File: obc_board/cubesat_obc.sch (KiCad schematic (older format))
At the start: 10 parts, among them J1 Conn_01x08_Female, J2 Conn_01x05_Female, J3 Conn_01x04_Female, J4 Conn_01x04_Female

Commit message: modify planes
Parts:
- renumbered J3 to ADC0, J4 to ADC1, J2 to SPI0, J1 to UART_FTDI0
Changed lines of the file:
@@
 $Descr A4 11693 8268
 encoding utf-8
-Sheet 1 8
+Sheet 1 9
 Title ""
 Date ""
@@
 S 1400 2300 1350 1100
 U 5F315FB6
-F0 "sensors" 50
-F1 "sensors.sch" 50
+F0 "temp_sensors" 50
+F1 "temp_sensors.sch" 50
 F2 "3V3" I L 1400 2500 50
 F3 "GND" I L 1400 2600 50
@@
 	7700 1150 8300 1150
 $Comp
-L Connector:Conn_01x04_Female J3
+L Connector:Conn_01x04_Female ADC0
 U 1 1 5F6F0159
 P 4400 7100
-F 0 "J3" H 4428 7076 50  0000 L CNN
+F 0 "ADC0" H 4428 7076 50  0000 L CNN
 F 1 "Conn_01x04_Female" H 4428 6985 50  0000 L CNN
 F 2 "Connector_Molex:Molex_PicoBlade_53261-0471_1x04-1MP_P1.25mm_Horizontal" H 4400 7100 50  0001 C CNN
@@
 	3700 7150 3700 7000
 $Comp
-L Connector:Conn_01x04_Female J4
+L Connector:Conn_01x04_Female ADC1
 U 1 1 5F6F5054
 P 6100 7100
-F 0 "J4" H 6128 7076 50  0000 L CNN
+F 0 "ADC1" H 6128 7076 50  0000 L CNN
 F 1 "Conn_01x04_Female" H 6128 6985 50  0000 L CNN
 F 2 "Connector_Molex:Molex_PicoBlade_53261-0471_1x04-1MP_P1.25mm_Horizontal" H 6100 7100 50  0001 C CNN
@@
 3V3_P
 $Comp
-L Connector:Conn_01x05_Female J2
+L Connector:Conn_01x05_Female SPI0
 U 1 1 5F3493AD
 P 7250 3050
-F 0 "J2" H 7278 3076 50  0000 L CNN
+F 0 "SPI0" H 7278 3076 50  0000 L CNN
 F 1 "Conn_01x05_Female" H 7278 2985 50  0000 L CNN
 F 2 "Connector_Molex:Molex_PicoBlade_53261-0571_1x05-1MP_P1.25mm_Horizontal" H 7250 3050 50  0001 C CNN
@@
 P 3200 6900
 AR Path="/5E7EC636/5F5D669F" Ref="J?"  Part="1"
-AR Path="/5F5D669F" Ref="J1"  Part="1"
-F 0 "J1" H 3092 6275 50  0000 C CNN
+AR Path="/5F5D669F" Ref="UART_FTDI0"  Part="1"
+F 0 "UART_FTDI0" H 3092 6275 50  0000 C CNN
 F 1 "Conn_01x08_Female" H 3092 6366 50  0000 C CNN
 F 2 "Connector_Molex:Molex_PicoBlade_53261-0871_1x08-1MP_P1.25mm_Horizontal" H 3200 6900 50  0001 C CNN
@@
 Text Label 3050 5600 0    50   ~ 0
 FAULT4
+$Sheet
+S 6750 5400 850  800
+U 5F9EB759
+F0 "imu" 50
+F1 "imu.sch" 50
+$EndSheet
 $EndSCHEMATC

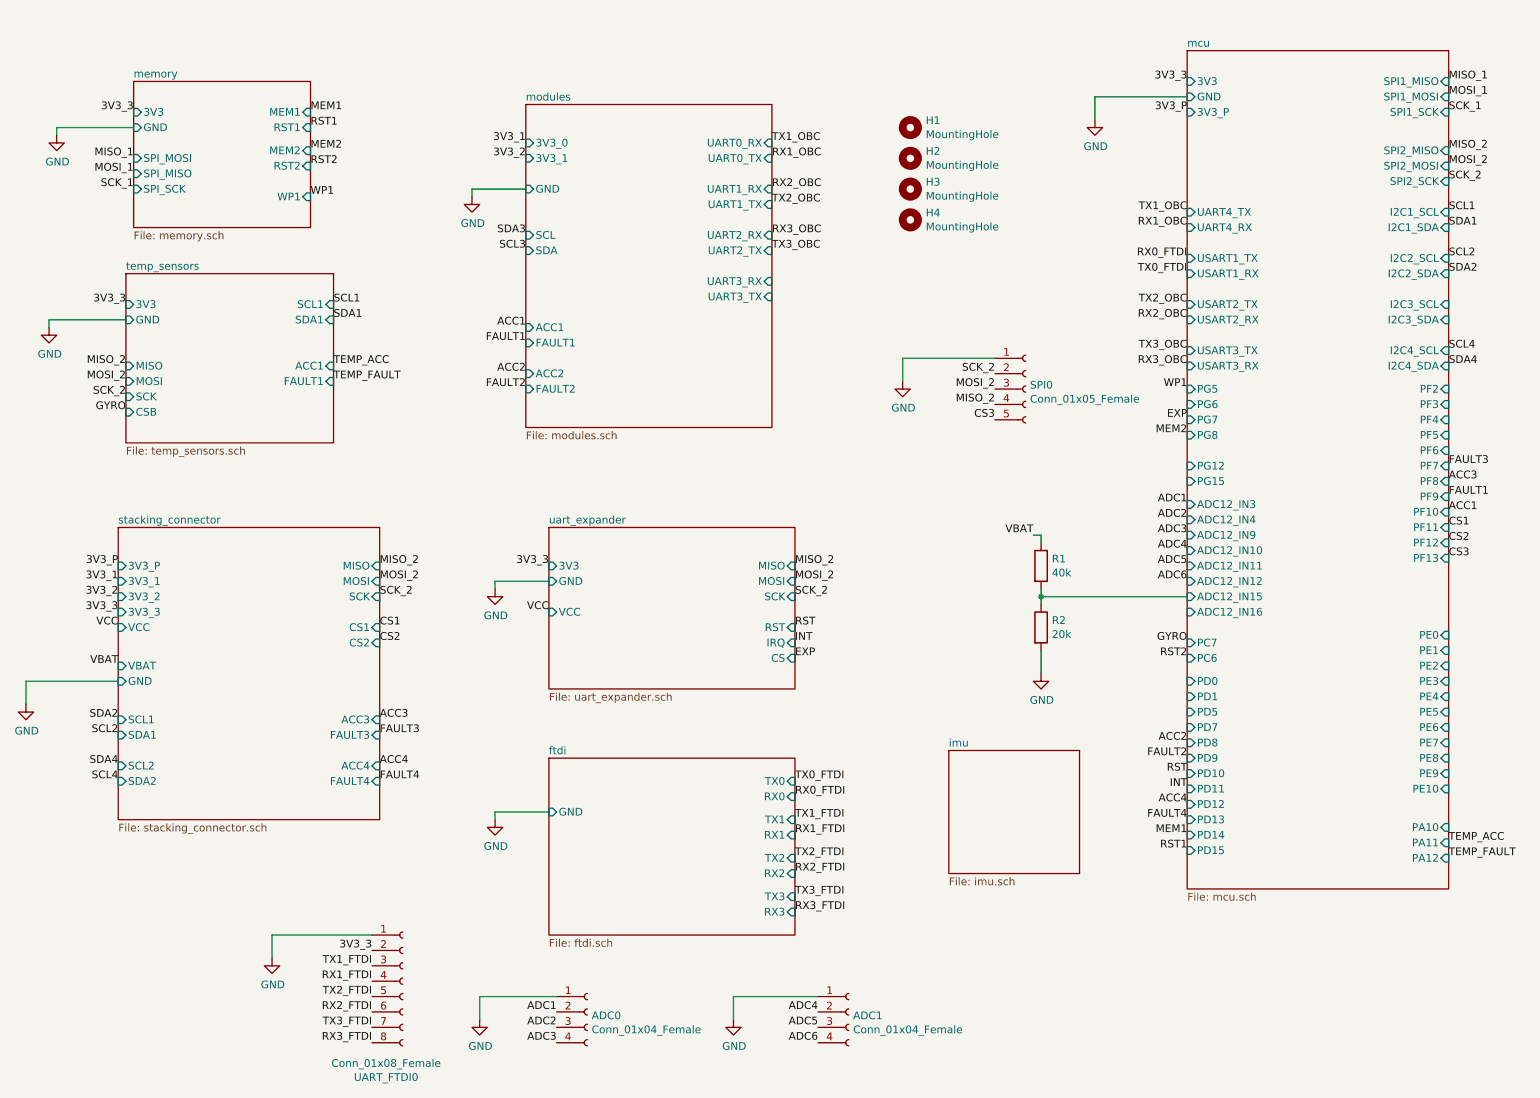
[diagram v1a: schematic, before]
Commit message: add imu and mux
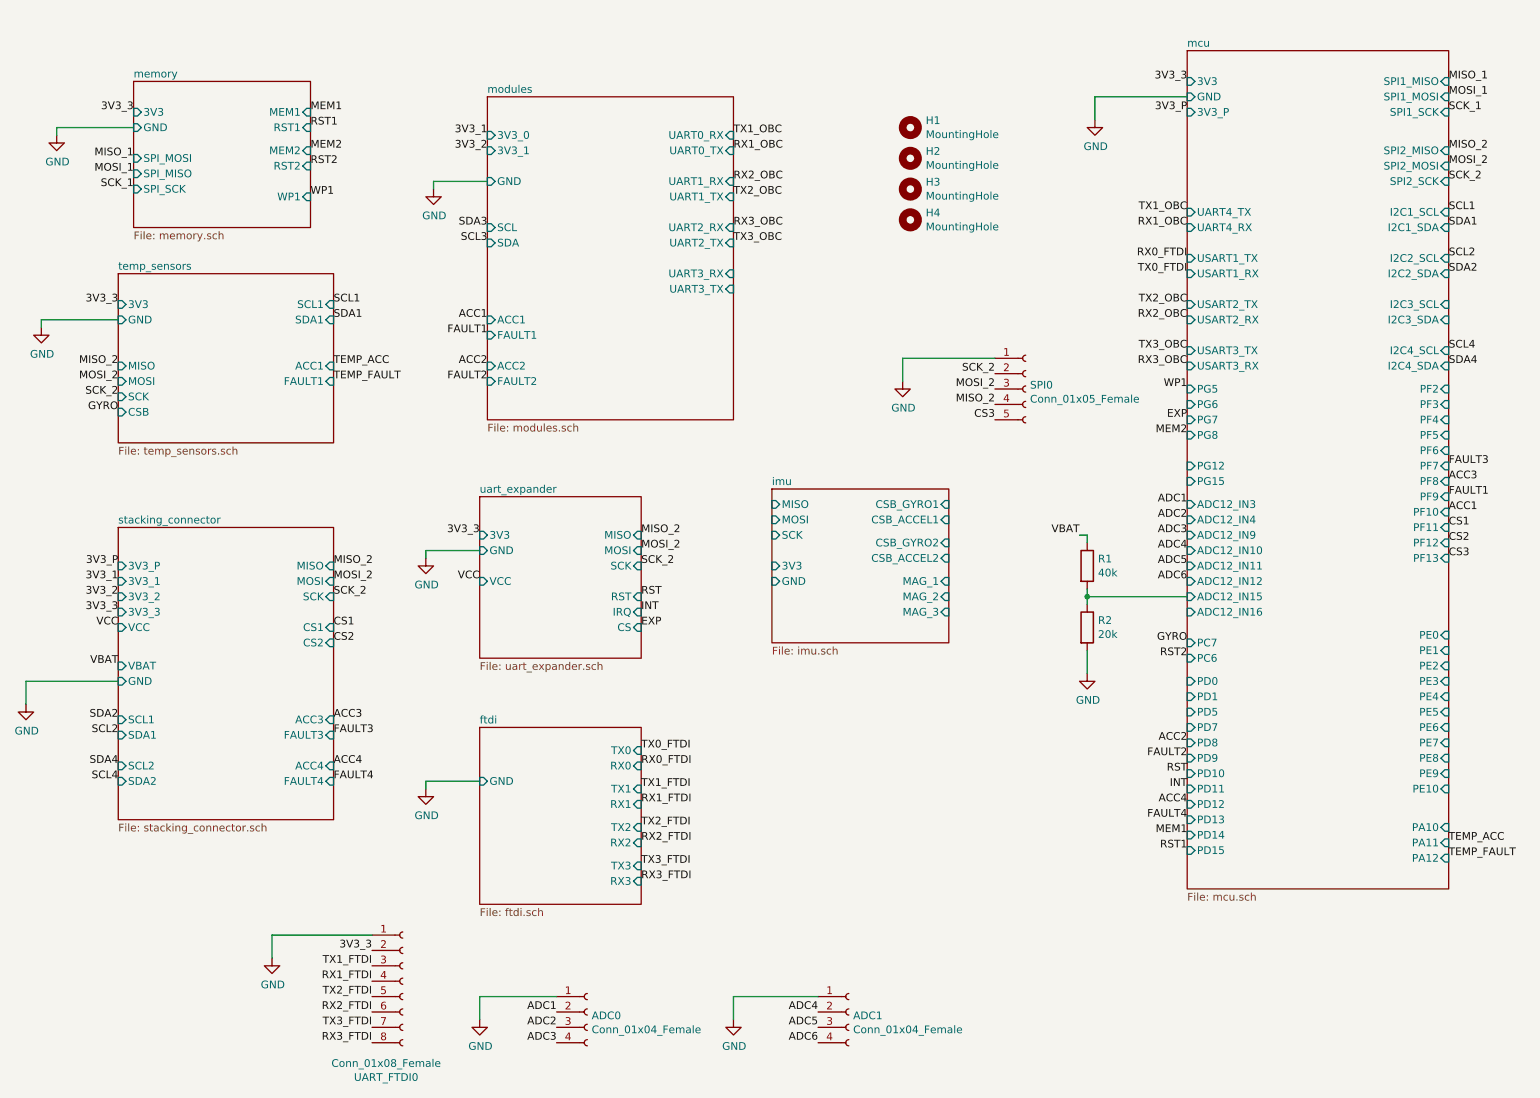
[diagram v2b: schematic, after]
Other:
- moved on the sheet: R1, R2

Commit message: added h bridge and magnetometers
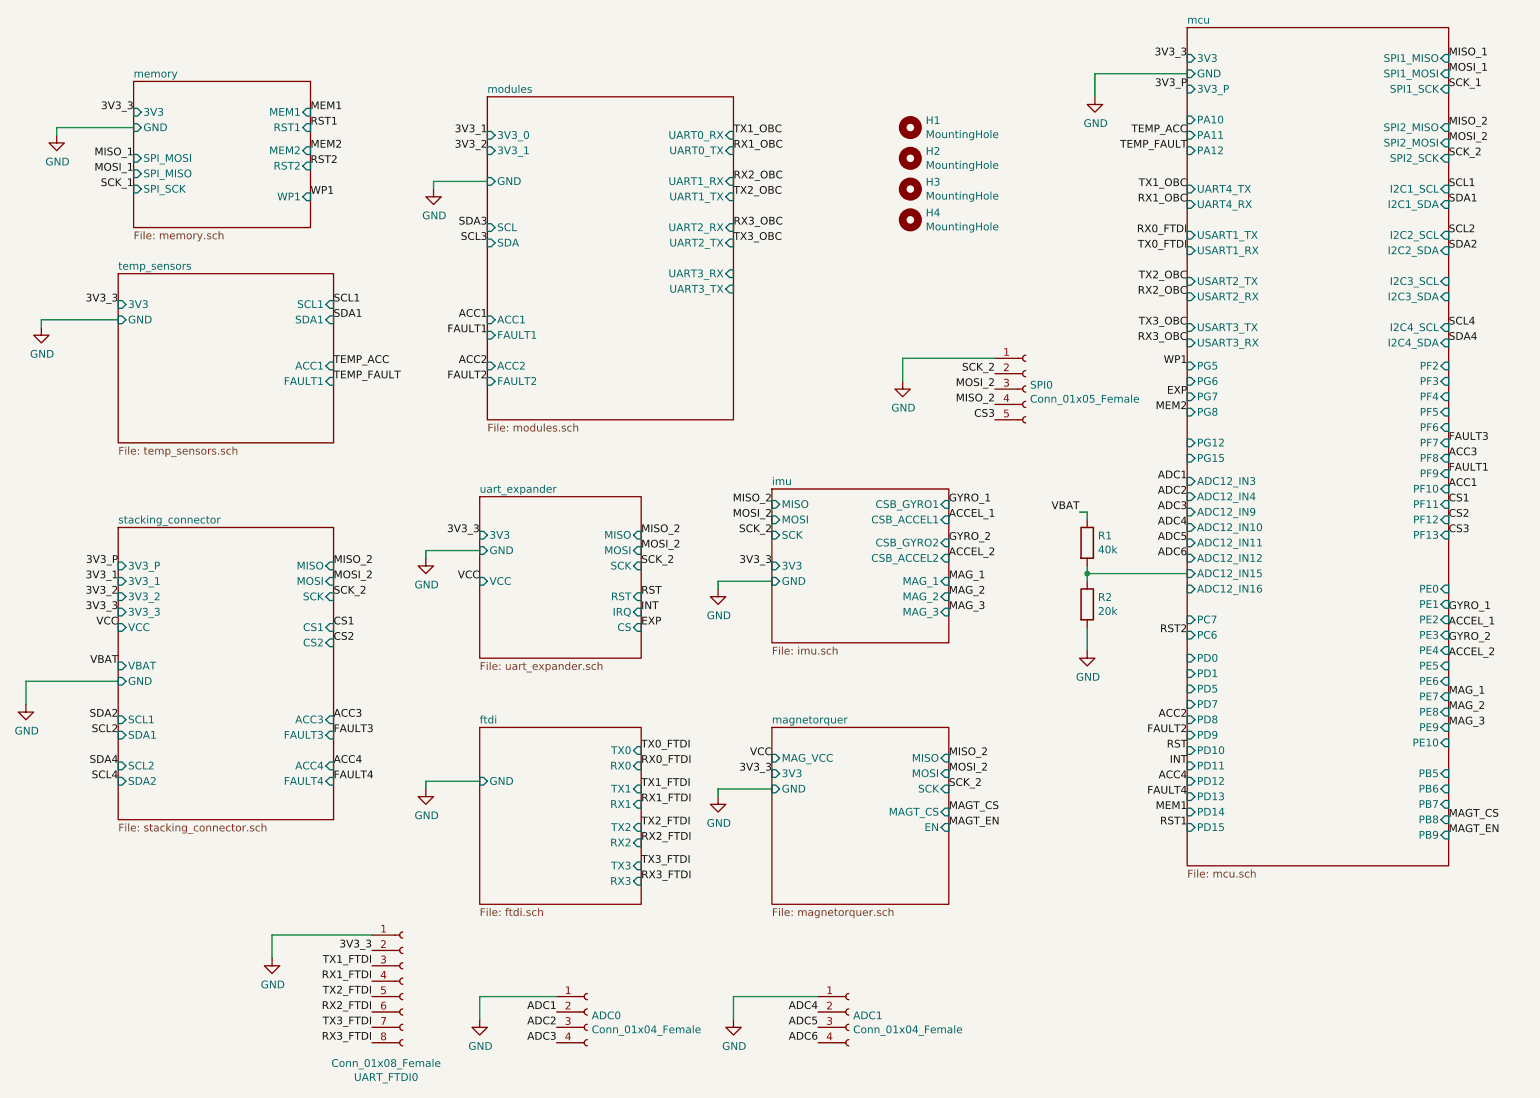
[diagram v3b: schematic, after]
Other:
- moved on the sheet: R1, R2

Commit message: reroute
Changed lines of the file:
@@
 F2 "3V3" I L 1350 2500 50
 F3 "GND" I L 1350 2600 50
-F8 "SCL1" I R 2750 2500 50
-F9 "SDA1" I R 2750 2600 50
-F10 "ACC1" I R 2750 2900 50
-F11 "FAULT1" I R 2750 3000 50
+F4 "SCL1" I R 2750 2500 50
+F5 "SDA1" I R 2750 2600 50
+F6 "ACC1" I R 2750 2900 50
+F7 "FAULT1" I R 2750 3000 50
 $EndSheet
 $Sheet
@@
 Text Label 2750 2900 0    50   ~ 0
 TEMP_ACC
-Text Label 8300 1400 2    50   ~ 0
+Text Label 8300 4800 2    50   ~ 0
 TEMP_ACC
 Text Label 2750 3000 0    50   ~ 0
 TEMP_FAULT
-Text Label 8300 1500 2    50   ~ 0
+Text Label 8300 4900 2    50   ~ 0
 TEMP_FAULT
 Text Label 3750 2600 2    50   ~ 0

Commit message: rerouted
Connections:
- net MISO_2: now also SPI0.2 (Pin_2); no longer SPI0.4 (Pin_4)
- net SCK_2: now also SPI0.4 (Pin_4); no longer SPI0.2 (Pin_2)
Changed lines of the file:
@@
 F18 "UART3_TX" I R 5350 2400 50
 $EndSheet
-Text Label 8300 5800 2    50   ~ 0
+Text Label 8300 2900 2    50   ~ 0
 MEM1
-Text Label 8300 3200 2    50   ~ 0
+Text Label 8300 3100 2    50   ~ 0
 MEM2
 Text Label 2600 1250 0    50   ~ 0
@@
 Text Label 8300 4650 2    50   ~ 0
 RST2
-Text Label 8300 2900 2    50   ~ 0
+Text Label 8300 5900 2    50   ~ 0
 WP1
-Text Label 8300 5900 2    50   ~ 0
+Text Label 8300 3000 2    50   ~ 0
 RST1
 Text Label 2600 1350 0    50   ~ 0
@@
 F 1 "Conn_01x04_Female" H 4428 6985 50  0000 L CNN
 F 2 "Connector_Molex:Molex_PicoBlade_53261-0471_1x04-1MP_P1.25mm_Horizontal" H 4400 7100 50  0001 C CNN
-F 3 "https://www.molex.com/pdm_docs/sd/532610471_sd.pdf" H 4400 7100 50  0001 C CNN
+F 3 "~" H 4400 7100 50  0001 C CNN
 F 4 "WM7622CT-ND" H 4400 7100 50  0001 C CNN "Digikey Part Number"
 	1    4400 7100
@@
 F 1 "Conn_01x04_Female" H 6128 6985 50  0000 L CNN
 F 2 "Connector_Molex:Molex_PicoBlade_53261-0471_1x04-1MP_P1.25mm_Horizontal" H 6100 7100 50  0001 C CNN
-F 3 "https://www.molex.com/pdm_docs/sd/532610471_sd.pdf" H 6100 7100 50  0001 C CNN
+F 3 "~" H 6100 7100 50  0001 C CNN
 F 4 "WM7622CT-ND" H 6100 7100 50  0001 C CNN "Digikey Part Number"
 	1    6100 7100
@@
 F 1 "Conn_01x05_Female" H 7278 2985 50  0000 L CNN
 F 2 "Connector_Molex:Molex_PicoBlade_53261-0571_1x05-1MP_P1.25mm_Horizontal" H 7250 3050 50  0001 C CNN
-F 3 "https://www.molex.com/pdm_docs/sd/532610571_sd.pdf" H 7250 3050 50  0001 C CNN
+F 3 "~" H 7250 3050 50  0001 C CNN
 F 4 "WM7623CT-ND" H 7250 3050 50  0001 C CNN "Digikey Part Number"
 	1    7250 3050
 	1    0    0    -1
 $EndComp
-Text Label 7050 2950 2    50   ~ 0
+Text Label 7050 3150 2    50   ~ 0
 SCK_2
 Text Label 7050 3050 2    50   ~ 0
 MOSI_2
-Text Label 7050 3150 2    50   ~ 0
+Text Label 7050 2950 2    50   ~ 0
 MISO_2
 Text Label 10000 3800 0    50   ~ 0
@@
 Text Label 7050 3250 2    50   ~ 0
 CS3
-Text Label 8300 3100 2    50   ~ 0
+Text Label 8300 5800 2    50   ~ 0
 EXP
 Text Label 3700 4300 2    50   ~ 0
@@
 F 1 "Conn_01x08_Female" H 3092 6366 50  0000 C CNN
 F 2 "Connector_Molex:Molex_PicoBlade_53261-0871_1x08-1MP_P1.25mm_Horizontal" H 3200 6900 50  0001 C CNN
-F 3 "https://www.molex.com/pdm_docs/sd/532610871_sd.pdf" H 3200 6900 50  0001 C CNN
+F 3 "~" H 3200 6900 50  0001 C CNN
 F 4 "WM7626CT-ND" H 3200 6900 50  0001 C CNN "Digikey Part Number"
 	1    3200 6900
@@
 F 1 "20k" H 7720 4405 50  0000 L CNN
 F 2 "Resistor_SMD:R_0603_1608Metric" V 7580 4450 50  0001 C CNN
-F 3 "http://www.vishay.com/docs/60026/ptn.pdf" H 7650 4450 50  0001 C CNN
+F 3 "~" H 7650 4450 50  0001 C CNN
 F 4 "764-1399-1-ND" H 7650 4450 50  0001 C CNN "Digikey Part Number"
 	1    7650 4450
@@
 F 1 "40k" H 7720 4005 50  0000 L CNN
 F 2 "Resistor_SMD:R_0603_1608Metric" V 7580 4050 50  0001 C CNN
-F 3 "http://www.vishay.com/docs/60024/pat.pdf" H 7650 4050 50  0001 C CNN
+F 3 "~" H 7650 4050 50  0001 C CNN
 F 4 "PAT40KACT-ND" H 7650 4050 50  0001 C CNN "Digikey Part Number"
 	1    7650 4050
@@
 Text Label 6750 4500 0    50   ~ 0
 MAG_3
-Text Label 10000 4600 0    50   ~ 0
+Text Label 10000 4650 0    50   ~ 0
 ACCEL_1
-Text Label 10000 4800 0    50   ~ 0
+Text Label 10000 4850 0    50   ~ 0
 ACCEL_2
-Text Label 10000 4700 0    50   ~ 0
+Text Label 10000 4750 0    50   ~ 0
 GYRO_2
-Text Label 10000 4500 0    50   ~ 0
+Text Label 10000 4550 0    50   ~ 0
 GYRO_1
-Text Label 10000 5050 0    50   ~ 0
+Text Label 8300 4550 2    50   ~ 0
 MAG_1
-Text Label 10000 5150 0    50   ~ 0
+Text Label 10000 5850 0    50   ~ 0
 MAG_2
 Text Label 10000 5250 0    50   ~ 0
@@
 Text Label 6750 5900 0    50   ~ 0
 MAGT_EN
-Text Label 10000 5850 0    50   ~ 0
+Text Label 10000 5650 0    50   ~ 0
 MAGT_CS
-Text Label 10000 5950 0    50   ~ 0
+Text Label 10000 5750 0    50   ~ 0
 MAGT_EN
 Wire Wire Line
